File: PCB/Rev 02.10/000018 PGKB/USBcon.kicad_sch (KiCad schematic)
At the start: 10 parts, among them J1 USB C

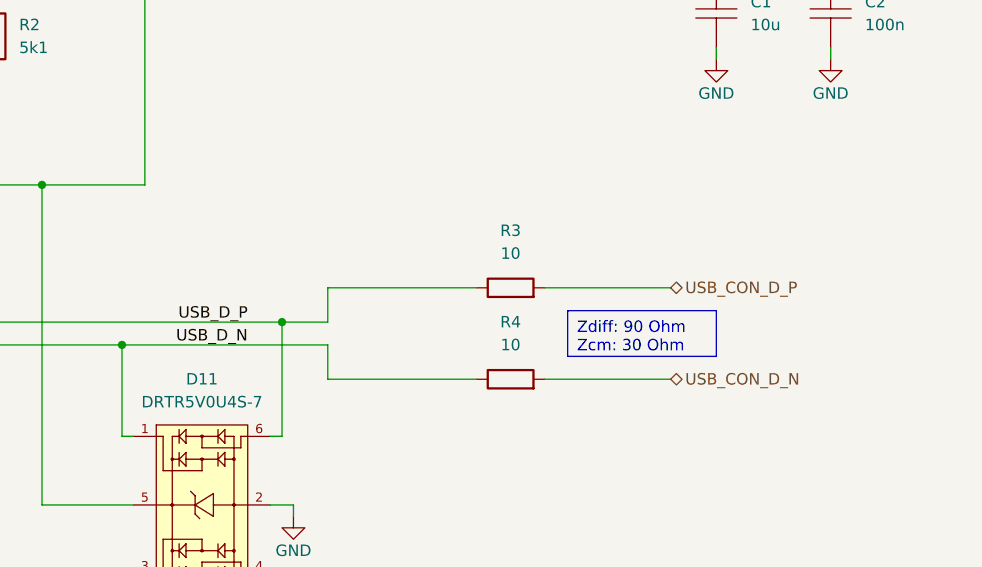
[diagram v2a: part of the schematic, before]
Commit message: Bugfixes for Rev 2
Oscillator, USB reversed, USB series resistors values
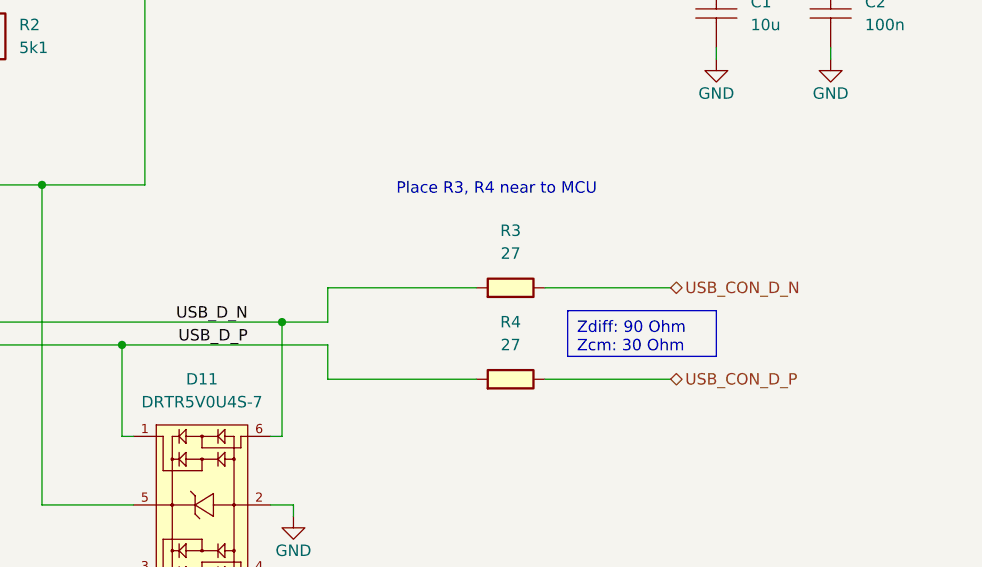
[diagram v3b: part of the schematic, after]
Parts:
- R3, R4: value R_0603_10_5% -> 27; footprint KD_Resistor:RESC1608X55N -> KD_Resistor:RESC1005X40N; symbol KD_Resistor:R_0603_10_5% -> KD_Resistor:R_0402_27_1%; Code 10 -> (none); MFG_PartNo WR06X100 JTL -> CR0402-FX-27R0GLF; Manufacturer Walsin Technology Corporation -> Bourns Inc.; Supplier_PartNo 1292-WR06X100JTLCT-ND -> CR0402-FX-27R0GLFCT-ND
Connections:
- net USB_CON_D_N: now also R3.2; no longer R4.2
- net USB_CON_D_P: now also R4.2; no longer R3.2
- net USB_D_N: now also D11.6, J1.A7 (D-), J1.B7 (D-), R3.1; no longer D11.1, J1.A6 (D+), J1.B6 (D+), R4.1
- net USB_D_P: now also D11.1, J1.A6 (D+), J1.B6 (D+), R4.1; no longer D11.6, J1.A7 (D-), J1.B7 (D-), R3.1
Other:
- note added: "Place R3, R4 near to MCU"
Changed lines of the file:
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@@
 		)
 	)
-	(label "CC2"
-		(at 104.14 53.34 0)
-		(fields_autoplaced yes)
+	(text "Place R3, R4 near to MCU"
+		(exclude_from_sim no)
+		(at 166.37 76.2 0)
 		(effects
 			(font
@@
 		)
 	)
-	(label "USB_D_P"
-		(at 149.86 90.17 180)
+	(label "CC2"
+		(at 104.14 53.34 0)
 		(fields_autoplaced yes)
 		(effects
@@
 				(size 1.27 1.27)
 			)
-			(justify right bottom)
-		)
-	)
-	(label "USB_D_N"
+			(justify left bottom)
+		)
+	)
+	(label "USB_D_P"
 		(at 149.86 92.71 180)
 		(fields_autoplaced yes)
@@
 		)
 	)
-	(label "CC1"
-		(at 104.14 50.8 0)
+	(label "USB_D_N"
+		(at 149.86 90.17 180)
 		(fields_autoplaced yes)
 		(effects
@@
 				(size 1.27 1.27)
 			)
+			(justify right bottom)
+		)
+	)
+	(label "CC1"
+		(at 104.14 50.8 0)
+		(fields_autoplaced yes)
+		(effects
+			(font
+				(size 1.27 1.27)
+			)
 			(justify left bottom)
+		)
+	)
+	(hierarchical_label "USB_CON_D_N"
+		(shape bidirectional)
+		(at 196.85 86.36 0)
+		(fields_autoplaced yes)
+		(effects
+			(font
+				(size 1.27 1.27)
+			)
+			(justify left)
+		)
+	)
+	(hierarchical_label "USB_CON_D_P"
+		(shape bidirectional)
+		(at 196.85 96.52 0)
+		(fields_autoplaced yes)
+		(effects
+			(font
+				(size 1.27 1.27)
+			)
+			(justify left)
 		)
 	)
@@
 		(shape input)
 		(at 238.76 50.8 0)
-		(fields_autoplaced yes)
-		(effects
-			(font
-				(size 1.27 1.27)
-			)
-			(justify left)
-		)
-	)
-	(hierarchical_label "USB_CON_D_N"
-		(shape bidirectional)
-		(at 196.85 96.52 0)
-		(fields_autoplaced yes)
-		(effects
-			(font
-				(size 1.27 1.27)
-			)
-			(justify left)
-		)
-	)
-	(hierarchical_label "USB_CON_D_P"
-		(shape bidirectional)
-		(at 196.85 86.36 0)
 		(fields_autoplaced yes)
 		(effects
@@
 	)
 	(symbol
-		(lib_id "KD_Resistor:R_0603_10_5%")
+		(lib_id "KD_Resistor:R_0402_27_1%")
 		(at 179.07 96.52 90)
 		(unit 1)
@@
 			)
 		)
-		(property "Value" "R_0603_10_5%"
+		(property "Value" "27"
+			(at 179.07 92.71 90)
+			(effects
+				(font
+					(size 1.27 1.27)
+				)
+			)
+		)
+		(property "Footprint" "KD_Resistor:RESC1005X40N"
+			(at 165.1 109.22 0)
+			(effects
+				(font
+					(size 1.27 1.27)
+				)
+				(justify left)
+				(hide yes)
+			)
+		)
+		(property "Datasheet" "https://www.bourns.com/docs/product-datasheets/cr.pdf?sfvrsn=574d41f6_14"
+			(at 167.64 109.22 0)
+			(effects
+				(font
+					(size 1.27 1.27)
+				)
+				(justify left)
+				(hide yes)
+			)
+		)
+		(property "Description" "RES SMD 27 OHM 1% 1/16W 0402"
 			(at 147.32 109.22 0)
 			(effects
@@
 			)
 		)
-		(property "Footprint" "KD_Resistor:RESC1608X55N"
-			(at 165.1 109.22 0)
-			(effects
-				(font
-					(size 1.27 1.27)
-				)
-				(justify left)
-				(hide yes)
-			)
-		)
-		(property "Datasheet" "https://www.te.com/commerce/DocumentDelivery/DDEController?Action=srchrtrv&DocNm=1773204-3&DocType=DS&DocLang=English"
-			(at 167.64 109.22 0)
-			(effects
-				(font
-					(size 1.27 1.27)
-				)
-				(justify left)
-				(hide yes)
-			)
-		)
-		(property "Description" ""
-			(at 179.07 96.52 0)
-			(effects
-				(font
-					(size 1.27 1.27)
-				)
-				(hide yes)
-			)
-		)
-		(property "Code" "10"
-			(at 179.07 92.71 90)
-			(effects
-				(font
-					(size 1.27 1.27)
-				)
-			)
-		)
-		(property "Manufacturer" "Walsin Technology Corporation"
+		(property "Manufacturer" "Bourns Inc."
 			(at 149.86 109.22 0)
 			(effects
@@
 			)
 		)
-		(property "MFG_PartNo" "WR06X100 JTL"
+		(property "MFG_PartNo" "CR0402-FX-27R0GLF"
 			(at 152.4 109.22 0)
 			(effects
@@
 			)
 		)
-		(property "Supplier_PartNo" "1292-WR06X100JTLCT-ND"
+		(property "Supplier_PartNo" "CR0402-FX-27R0GLFCT-ND"
 			(at 157.48 109.22 0)
 			(effects
@@
 	)
 	(symbol
-		(lib_id "KD_Resistor:R_0603_10_5%")
+		(lib_id "KD_Resistor:R_0402_27_1%")
 		(at 179.07 86.36 90)
 		(unit 1)
@@
 			)
 		)
-		(property "Value" "R_0603_10_5%"
+		(property "Value" "27"
+			(at 179.07 82.55 90)
+			(effects
+				(font
+					(size 1.27 1.27)
+				)
+			)
+		)
+		(property "Footprint" "KD_Resistor:RESC1005X40N"
+			(at 165.1 99.06 0)
+			(effects
+				(font
+					(size 1.27 1.27)
+				)
+				(justify left)
+				(hide yes)
+			)
+		)
+		(property "Datasheet" "https://www.bourns.com/docs/product-datasheets/cr.pdf?sfvrsn=574d41f6_14"
+			(at 167.64 99.06 0)
+			(effects
+				(font
+					(size 1.27 1.27)
+				)
+				(justify left)
+				(hide yes)
+			)
+		)
+		(property "Description" "RES SMD 27 OHM 1% 1/16W 0402"
 			(at 147.32 99.06 0)
 			(effects
@@
 			)
 		)
-		(property "Footprint" "KD_Resistor:RESC1608X55N"
-			(at 165.1 99.06 0)
-			(effects
-				(font
-					(size 1.27 1.27)
-				)
-				(justify left)
-				(hide yes)
-			)
-		)
-		(property "Datasheet" "https://www.te.com/commerce/DocumentDelivery/DDEController?Action=srchrtrv&DocNm=1773204-3&DocType=DS&DocLang=English"
-			(at 167.64 99.06 0)
-			(effects
-				(font
-					(size 1.27 1.27)
-				)
-				(justify left)
-				(hide yes)
-			)
-		)
-		(property "Description" ""
-			(at 179.07 86.36 0)
-			(effects
-				(font
-					(size 1.27 1.27)
-				)
-				(hide yes)
-			)
-		)
-		(property "Code" "10"
-			(at 179.07 82.55 90)
-			(effects
-				(font
-					(size 1.27 1.27)
-				)
-			)
-		)
-		(property "Manufacturer" "Walsin Technology Corporation"
+		(property "Manufacturer" "Bourns Inc."
 			(at 149.86 99.06 0)
 			(effects
@@
 			)
 		)
-		(property "MFG_PartNo" "WR06X100 JTL"
+		(property "MFG_PartNo" "CR0402-FX-27R0GLF"
 			(at 152.4 99.06 0)
 			(effects
@@
 			)
 		)
-		(property "Supplier_PartNo" "1292-WR06X100JTLCT-ND"
+		(property "Supplier_PartNo" "CR0402-FX-27R0GLFCT-ND"
 			(at 157.48 99.06 0)
 			(effects

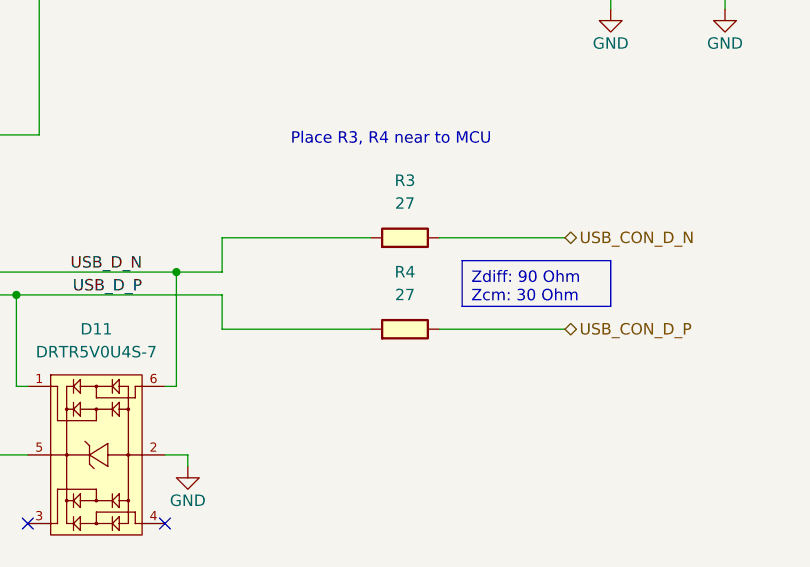
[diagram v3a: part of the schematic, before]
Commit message: Update USBcon.kicad_sch
Changed back to 0603 components
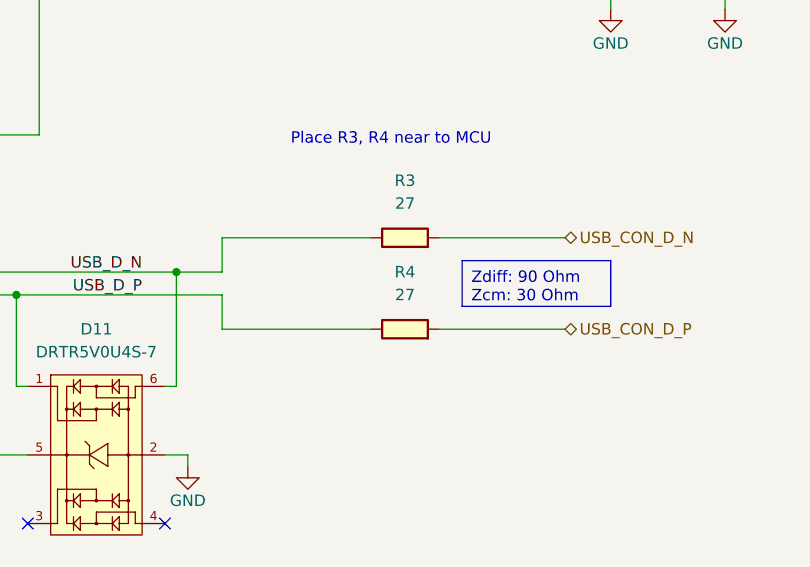
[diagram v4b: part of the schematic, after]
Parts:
- R3, R4: footprint KD_Resistor:RESC1005X40N -> KD_Resistor:RESC1608X55N; symbol KD_Resistor:R_0402_27_1% -> KD_Resistor:R_0603_27_1%; MFG_PartNo CR0402-FX-27R0GLF -> CR0603-FX-27R0ELF; Price 0.01 -> 0.02; Supplier_PartNo CR0402-FX-27R0GLFCT-ND -> CR0603-FX-27R0ELFCT-ND
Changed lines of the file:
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@@
 	)
 	(symbol
-		(lib_id "KD_Resistor:R_0402_27_1%")
+		(lib_id "KD_Resistor:R_0603_27_1%")
 		(at 179.07 96.52 90)
 		(unit 1)
@@
 			)
 		)
-		(property "Footprint" "KD_Resistor:RESC1005X40N"
+		(property "Footprint" "KD_Resistor:RESC1608X55N"
 			(at 165.1 109.22 0)
 			(effects
@@
 			)
 		)
-		(property "Description" "RES SMD 27 OHM 1% 1/16W 0402"
+		(property "Description" "RES SMD 27 OHM 1% 1/10W 0603"
 			(at 147.32 109.22 0)
 			(effects
@@
 			)
 		)
-		(property "MFG_PartNo" "CR0402-FX-27R0GLF"
+		(property "MFG_PartNo" "CR0603-FX-27R0ELF"
 			(at 152.4 109.22 0)
 			(effects
@@
 			)
 		)
-		(property "Supplier_PartNo" "CR0402-FX-27R0GLFCT-ND"
+		(property "Supplier_PartNo" "CR0603-FX-27R0ELFCT-ND"
 			(at 157.48 109.22 0)
 			(effects
@@
 			)
 		)
-		(property "Price" "0.01"
+		(property "Price" "0.02"
 			(at 162.56 109.22 0)
 			(effects
@@
 	)
 	(symbol
-		(lib_id "KD_Resistor:R_0402_27_1%")
+		(lib_id "KD_Resistor:R_0603_27_1%")
 		(at 179.07 86.36 90)
 		(unit 1)
@@
 			)
 		)
-		(property "Footprint" "KD_Resistor:RESC1005X40N"
+		(property "Footprint" "KD_Resistor:RESC1608X55N"
 			(at 165.1 99.06 0)
 			(effects
@@
 			)
 		)
-		(property "Description" "RES SMD 27 OHM 1% 1/16W 0402"
+		(property "Description" "RES SMD 27 OHM 1% 1/10W 0603"
 			(at 147.32 99.06 0)
 			(effects
@@
 			)
 		)
-		(property "MFG_PartNo" "CR0402-FX-27R0GLF"
+		(property "MFG_PartNo" "CR0603-FX-27R0ELF"
 			(at 152.4 99.06 0)
 			(effects
@@
 			)
 		)
-		(property "Supplier_PartNo" "CR0402-FX-27R0GLFCT-ND"
+		(property "Supplier_PartNo" "CR0603-FX-27R0ELFCT-ND"
 			(at 157.48 99.06 0)
 			(effects
@@
 			)
 		)
-		(property "Price" "0.01"
+		(property "Price" "0.02"
 			(at 162.56 99.06 0)
 			(effects

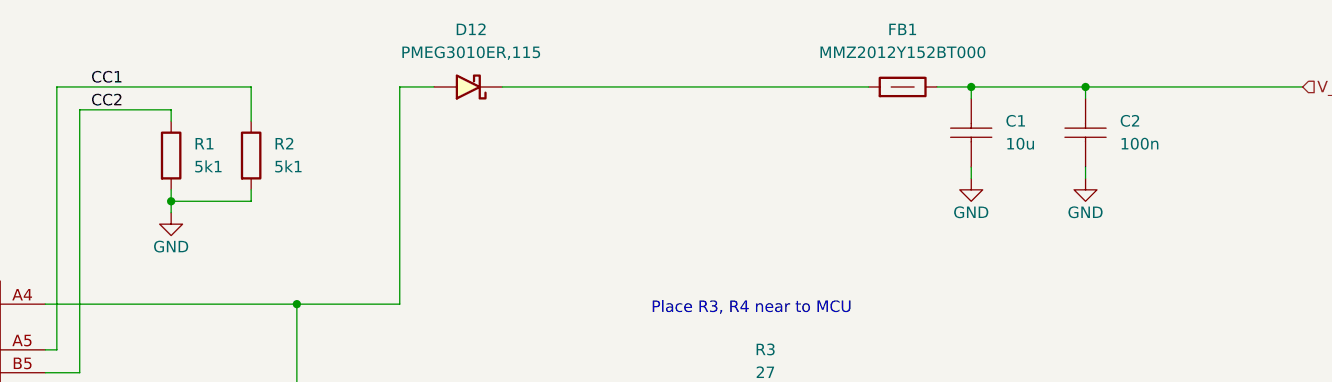
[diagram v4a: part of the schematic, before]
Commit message: Resolved DRC problems
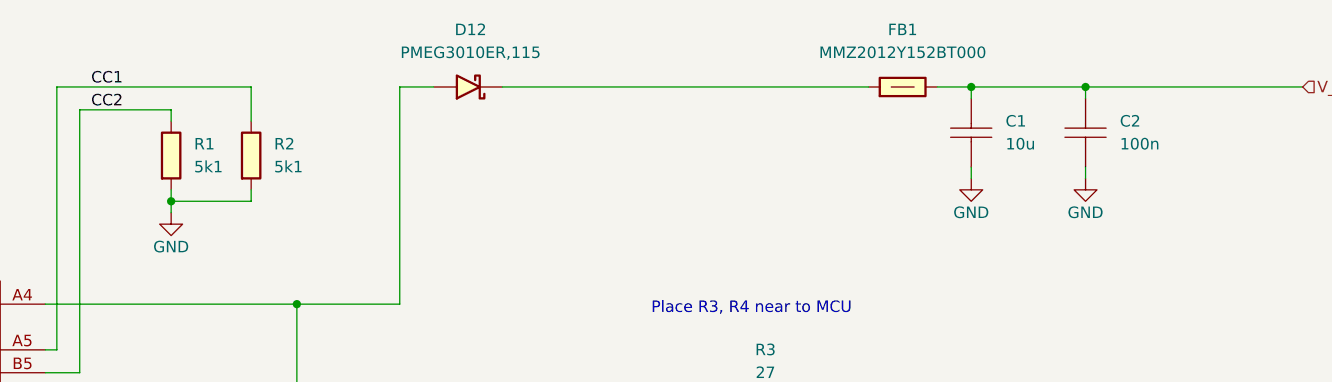
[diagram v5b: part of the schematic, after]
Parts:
- C1: symbol KD_Capacitor:C_1206_10u_X5R_50V_automotive -> KD_Capacitor:C_1206_10u_X7R_16V; MFG_PartNo GRT31CR61H106ME01L -> CL31B106MOHNNNE; Manufacturer Murata Electronics -> Samsung Electro-Mechanics; Price 0.30 -> 0.10; Supplier_PartNo 490-12457-1-ND -> 1276-6641-1-ND
- FB1: value Ferrite_500mA_TDK_MMZ2012Y152BT000 -> MMZ2012Y152BT000; Code MMZ2012Y152BT000 -> (none)
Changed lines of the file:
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@@
 		(fields_autoplaced yes)
 		(property "Reference" "R1"
-			(at 115.57 57.15 0)
+			(at 115.57 57.1499 0)
 			(effects
 				(font
@@
 			)
 		)
-		(property "Description" ""
+		(property "Description" "RES 5.1K OHM 5% 1/10W 0603"
 			(at 113.03 58.42 0)
 			(effects
@@
 		)
 		(property "Code" "5k1"
-			(at 115.57 59.69 0)
+			(at 115.57 59.6899 0)
 			(effects
 				(font
@@
 	)
 	(symbol
-		(lib_id "KD_Capacitor:C_1206_10u_X5R_50V_automotive")
+		(lib_id "KD_Capacitor:C_1206_10u_X7R_16V")
 		(at 201.93 55.88 0)
 		(unit 1)
@@
 		(fields_autoplaced yes)
 		(property "Reference" "C1"
-			(at 205.74 54.61 0)
+			(at 205.74 54.6099 0)
 			(effects
 				(font
@@
 			)
 		)
-		(property "Datasheet" "https://search.murata.co.jp/Ceramy/image/img/A01X/G101/ENG/GRT31CR61H106ME01-01.pdf"
+		(property "Datasheet" "https://www.samsungsem.com/kr/support/product-search/mlcc/CL31B106MOHNNNE.jsp"
 			(at 189.23 44.45 0)
 			(effects
@@
 			)
 		)
-		(property "Description" ""
+		(property "Description" "Capacitor"
 			(at 201.93 55.88 0)
 			(effects
@@
 			)
 		)
-		(property "Code" "10u"
-			(at 205.74 57.15 0)
-			(effects
-				(font
-					(size 1.27 1.27)
-				)
-				(justify left)
-			)
-		)
-		(property "Manufacturer" "Murata Electronics"
+		(property "Manufacturer" "Samsung Electro-Mechanics"
 			(at 189.23 26.67 0)
 			(effects
@@
 			)
 		)
-		(property "MFG_PartNo" "GRT31CR61H106ME01L"
+		(property "MFG_PartNo" "CL31B106MOHNNNE"
 			(at 189.23 29.21 0)
 			(effects
@@
 			)
 		)
-		(property "Supplier_PartNo" "490-12457-1-ND"
+		(property "Supplier_PartNo" "1276-6641-1-ND"
 			(at 189.23 34.29 0)
 			(effects
@@
 			)
 		)
-		(property "Price" "0.30"
+		(property "Price" "0.10"
 			(at 189.23 39.37 0)
 			(effects
@@
 				(justify left)
 				(hide yes)
+			)
+		)
+		(property "Code" "10u"
+			(at 205.74 57.1499 0)
+			(effects
+				(font
+					(size 1.27 1.27)
+				)
+				(justify left)
 			)
 		)
@@
 			)
 		)
-		(property "Description" ""
+		(property "Description" "Power symbol creates a global label with name \"GND\" , ground"
 			(at 113.03 64.77 0)
 			(effects
@@
 			)
 		)
-		(property "Description" ""
+		(property "Description" "TVS DIODE 5.5VWM SOT363"
 			(at 144.78 110.49 0)
 			(effects
@@
 			)
 		)
-		(property "Description" ""
+		(property "Description" "Power symbol creates a global label with name \"GND\" , ground"
 			(at 83.82 143.51 0)
 			(effects
@@
 			)
 		)
-		(property "Description" ""
+		(property "Description" "Power symbol creates a global label with name \"GND\" , ground"
 			(at 76.2 143.51 0)
 			(effects
@@
 			)
 		)
-		(property "Description" ""
+		(property "Description" "Power symbol creates a global label with name \"GND\" , ground"
 			(at 154.94 111.76 0)
 			(effects
@@
 			)
 		)
-		(property "Value" "Ferrite_500mA_TDK_MMZ2012Y152BT000"
-			(at 157.48 63.5 0)
-			(effects
-				(font
-					(size 1.27 1.27)
-				)
-				(justify left)
-				(hide yes)
+		(property "Value" "MMZ2012Y152BT000"
+			(at 194.31 46.99 90)
+			(effects
+				(font
+					(size 1.27 1.27)
+				)
 			)
 		)
@@
 			)
 		)
-		(property "Description" ""
-			(at 194.31 50.8 0)
-			(effects
-				(font
-					(size 1.27 1.27)
-				)
-				(hide yes)
-			)
-		)
-		(property "Code" "MMZ2012Y152BT000"
-			(at 194.31 46.99 90)
-			(effects
-				(font
-					(size 1.27 1.27)
-				)
+		(property "Description" "FERRITE BEAD 1.5 KOHM 0805 1LN"
+			(at 157.48 63.5 0)
+			(effects
+				(font
+					(size 1.27 1.27)
+				)
+				(justify left)
+				(hide yes)
 			)
 		)
@@
 		(fields_autoplaced yes)
 		(property "Reference" "D12"
-			(at 146.3675 44.45 0)
+			(at 146.304 44.45 0)
 			(effects
 				(font
@@
 			)
 		)
-		(property "Description" ""
+		(property "Description" "DIODE SCHOTTKY 30V 1A SOD123W"
 			(at 146.05 50.8 0)
 			(effects
@@
 		)
 		(property "Code" "PMEG3010ER,115"
-			(at 146.3675 46.99 0)
+			(at 146.304 46.99 0)
 			(effects
 				(font
@@
 		(fields_autoplaced yes)
 		(property "Reference" "C2"
-			(at 218.44 54.61 0)
+			(at 218.44 54.6099 0)
 			(effects
 				(font
@@
 		)
 		(property "Value" "100n"
-			(at 218.44 57.15 0)
+			(at 218.44 57.1499 0)
 			(effects
 				(font
@@
 			)
 		)
-		(property "Description" ""
+		(property "Description" "CAP CER 0.1UF 50V X7R 0603"
 			(at 214.63 55.88 0)
 			(effects
@@
 			)
 		)
-		(property "Description" ""
+		(property "Description" "Power symbol creates a global label with name \"GND\" , ground"
 			(at 214.63 60.96 0)
 			(effects
@@
 		(fields_autoplaced yes)
 		(property "Reference" "R2"
-			(at 124.46 57.15 0)
+			(at 124.46 57.1499 0)
 			(effects
 				(font
@@
 			)
 		)
-		(property "Description" ""
+		(property "Description" "RES 5.1K OHM 5% 1/10W 0603"
 			(at 121.92 58.42 0)
 			(effects
@@
 		)
 		(property "Code" "5k1"
-			(at 124.46 59.69 0)
+			(at 124.46 59.6899 0)
 			(effects
 				(font
@@
 			)
 		)
-		(property "Description" ""
+		(property "Description" "Power symbol creates a global label with name \"GND\" , ground"
 			(at 201.93 60.96 0)
 			(effects
@@
 			)
 		)
-		(property "Description" ""
+		(property "Description" "CONN RCPT USB2.0 TYPE C 16+8POS"
 			(at 99.06 74.93 0)
 			(effects
